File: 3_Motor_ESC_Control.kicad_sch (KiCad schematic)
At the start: 14 parts, among them J20 ESC_HEADER, J21 SERVO_HEADER

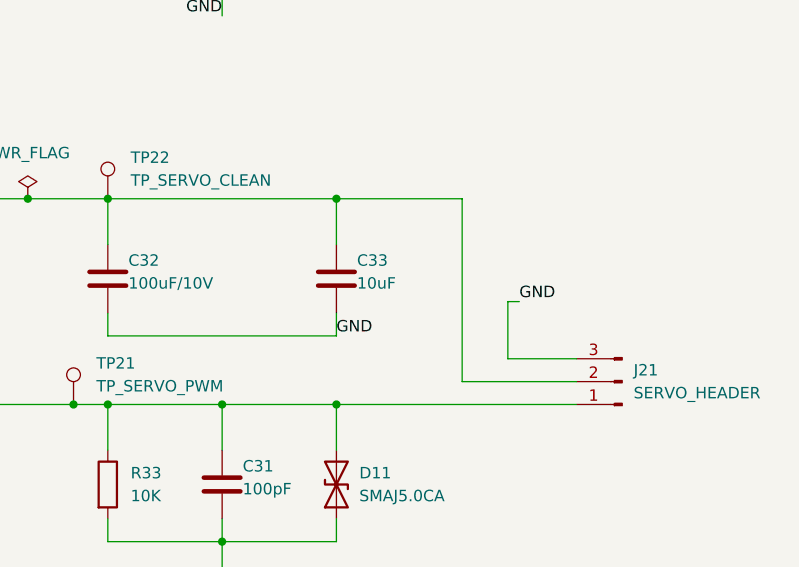
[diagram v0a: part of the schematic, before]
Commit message: Updated BOM. Initial review and corrections
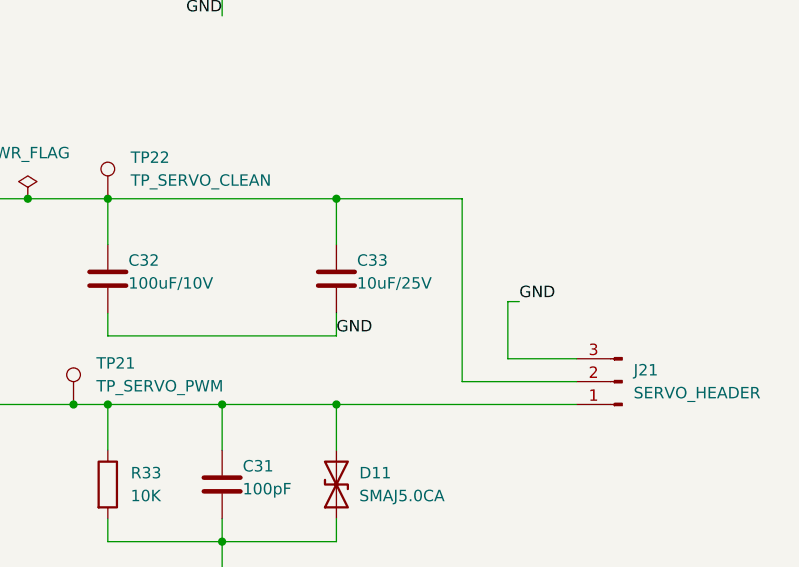
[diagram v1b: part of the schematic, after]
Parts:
- C30, C31: LCSC C1632 -> C14858
- C32: footprint Capacitor_SMD:C_0805_2012Metric -> Capacitor_THT:CP_Radial_D5.0mm_P2.00mm; now left out of the parts list
- C33: value 10uF -> 10uF/25V; LCSC C13585 -> C6119815
- D10, D11: LCSC C52923 -> C83324
- FB30: LCSC C1015 -> C16902
- J20, J21, TP20, TP21, TP22: now left out of the parts list
- R31, R33: LCSC C17902 -> C15401

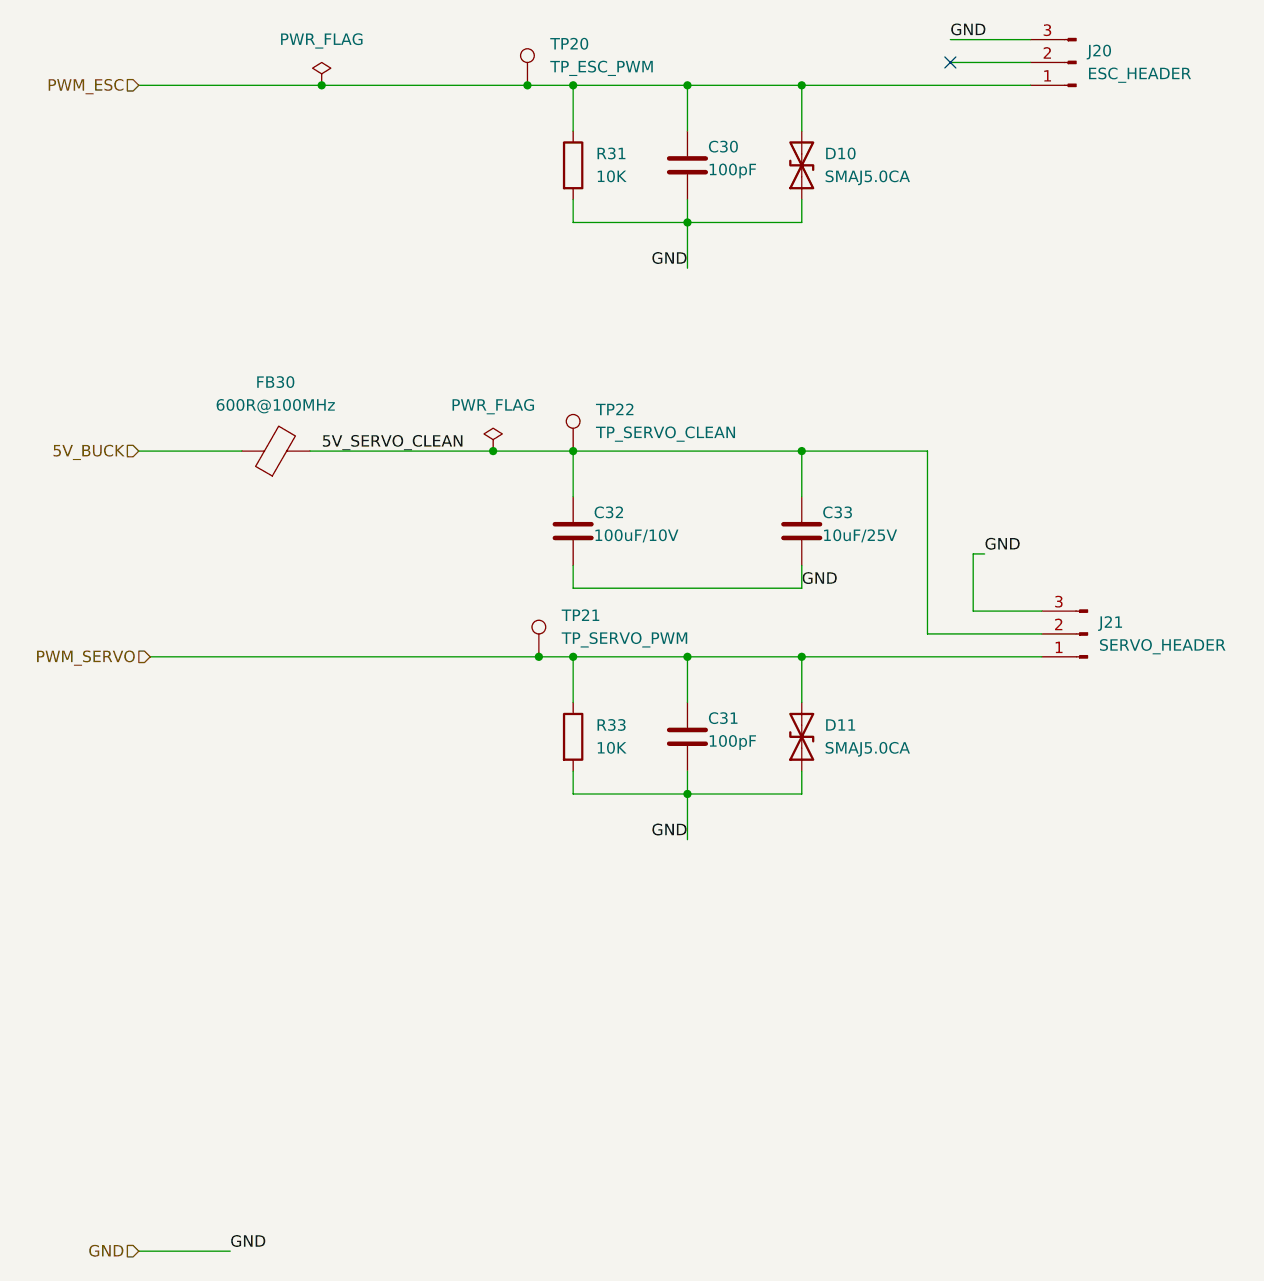
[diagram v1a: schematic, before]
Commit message: Cleaned up schematic. Added mounting holes.
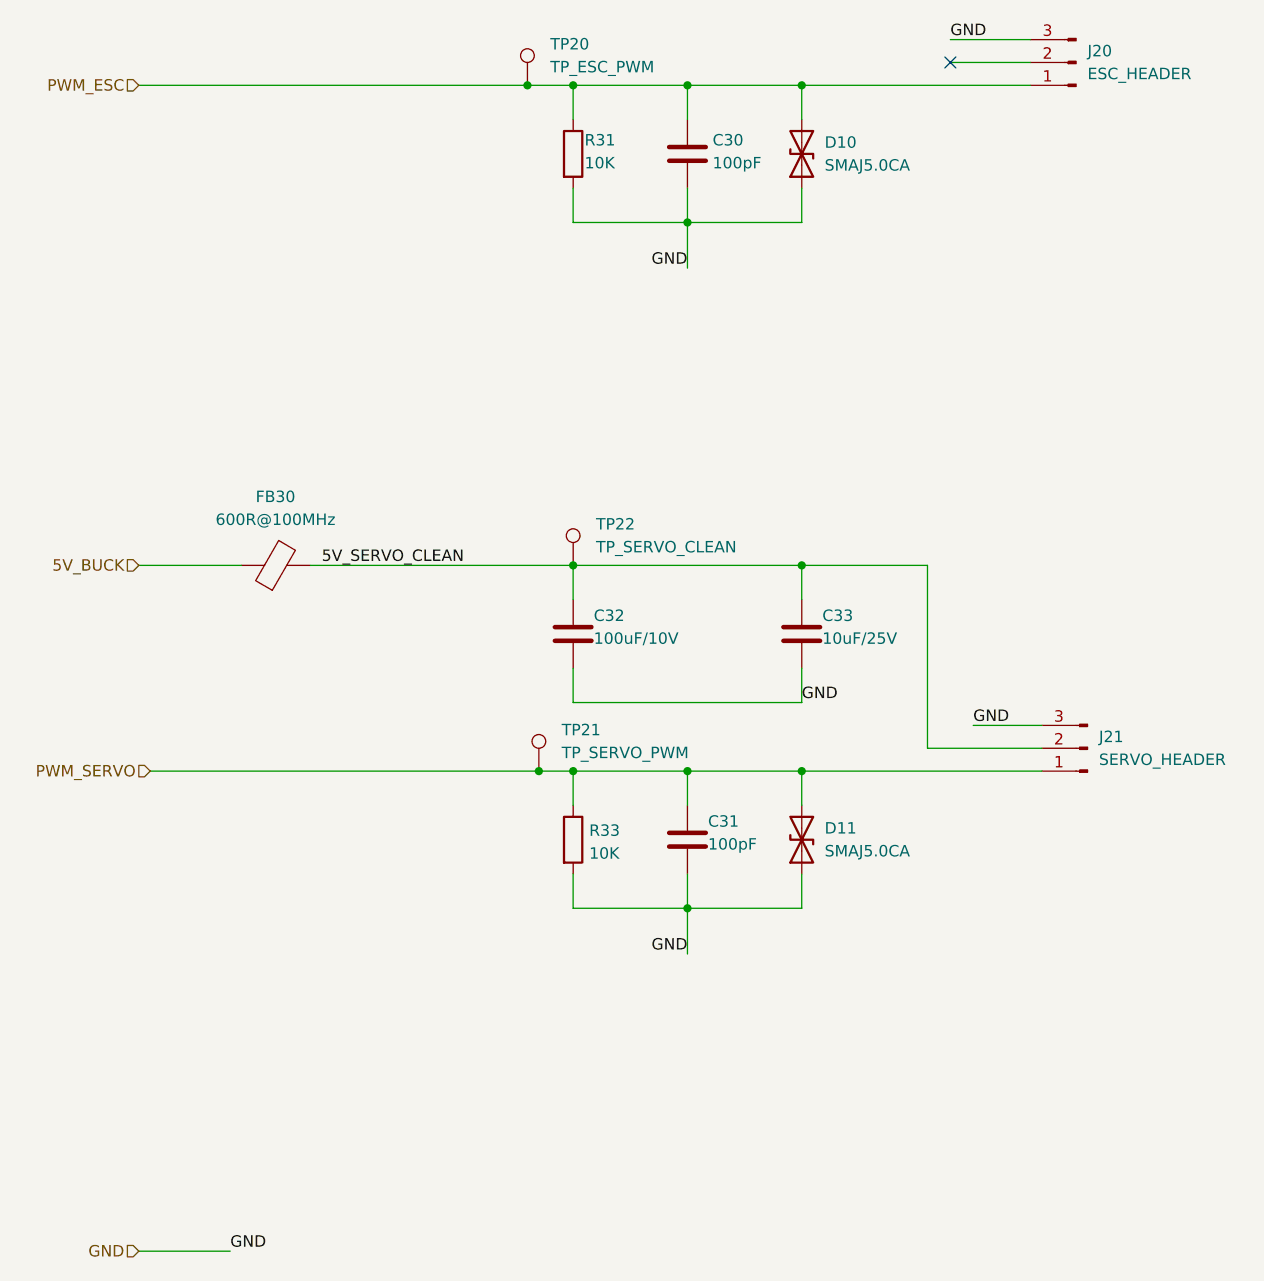
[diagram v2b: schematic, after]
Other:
- moved on the sheet: C30, C31, C32, C33, D10, D11, FB30, J21, R31, R33, TP21, TP22
